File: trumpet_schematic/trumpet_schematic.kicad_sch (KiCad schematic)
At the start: 17 parts, among them J1 LCD, Q1 NPN, SW1 SW_Push, SW10 SW_Push, SW2 SW_Push, SW3 SW_Push, SW4 SW_Push, SW5 SW_Push, SW6 SW_Push, SW7 SW_Push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

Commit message: song array (swappable)
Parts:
- R2: value R -> 20Ω
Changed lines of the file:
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@@
 			)
 		)
-		(property "Value" "R"
+		(property "Value" "20Ω"
 			(at 77.47 99.06 90)
 			(effects

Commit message: lcd start
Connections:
- net VCC: no longer J1.VDD (Pin_2), R3.2, R4.1
- new net VCC 5V: J1.VDD (Pin_2), R3.2, R4.1
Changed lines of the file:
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@@
 		)
 	)
-	(label "VCC"
+	(label "VCC 5V"
 		(at 152.4 81.28 0)
 		(effects

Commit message: lcd progress
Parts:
- removed R3: 5kΩ, symbol Device:R
- added R5: R_Variable, symbol Device:R_Variable
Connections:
- net VCC 5V: now also R5.1
- net at J1.VO (Pin_3): now also R5.2
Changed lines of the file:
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@@
+	)
+	(symbol
+		(lib_id "Device:R_Variable")
+		(at 161.29 91.44 90)
+		(unit 1)
+		(exclude_from_sim no)
+		(in_bom yes)
+		(on_board yes)
+		(dnp no)
+		(fields_autoplaced yes)
+		(property "Reference" "R5"
+			(at 161.29 83.82 90)
+			(effects
+				(font
+					(size 1.27 1.27)
+				)
+			)
+		)
+		(property "Value" "R_Variable"
+			(at 161.29 86.36 90)
+			(effects
+				(font
+					(size 1.27 1.27)
+				)
+			)
+		)
+		(property "Footprint" ""
+			(at 161.29 93.218 90)
+			(effects
+				(font
+					(size 1.27 1.27)
+				)
+				(hide yes)
+			)
+		)
+		(property "Datasheet" "~"
+			(at 161.29 91.44 0)
+			(effects
+				(font
+					(size 1.27 1.27)
+				)
+				(hide yes)
+			)
+		)
+		(property "Description" "Variable resistor"
+			(at 161.29 91.44 0)
+			(effects
+				(font
+					(size 1.27 1.27)
+				)
+				(hide yes)
+			)
+		)
+		(pin "1"
+		)
+		(pin "2"
+		)
+		(instances
+			(project ""
+				(path "/72e6d7f3-c76a-4c03-a31b-775dd92d8425"
+					(reference "R5")
+					(unit 1)
+				)
+			)
+		)
 	)
 	(symbol
@@
 					(unit 1)
 				)
-			)
-		)
-	)
-	(symbol
-		(lib_id "Device:R")
-		(at 161.29 91.44 270)
-		(unit 1)
-		(exclude_from_sim no)
-		(in_bom yes)
-		(on_board yes)
-		(dnp no)
-		(fields_autoplaced yes)
-		(property "Reference" "R3"
-			(at 161.29 85.09 90)
-			(effects
-				(font
-					(size 1.27 1.27)
-				)
-			)
-		)
-		(property "Value" "5kΩ"
-			(at 161.29 87.63 90)
-			(effects
-				(font
-					(size 1.27 1.27)
-				)
-			)
-		)
-		(property "Footprint" ""
-			(at 161.29 89.662 90)
-			(effects
-				(font
-					(size 1.27 1.27)
-				)
-				(hide yes)
-			)
-		)
-		(property "Datasheet" "~"
-			(at 161.29 91.44 0)
-			(effects
-				(font
-					(size 1.27 1.27)
-				)
-				(hide yes)
-			)
-		)
-		(property "Description" "Resistor"
-			(at 161.29 91.44 0)
-			(effects
-				(font
-					(size 1.27 1.27)
-				)
-				(hide yes)
-			)
-		)
-		(pin "1"
-		)
-		(pin "2"
-		)
-		(instances
-			(project ""
-				(path "/72e6d7f3-c76a-4c03-a31b-775dd92d8425"
-					(reference "R3")
-					(unit 1)
-				)

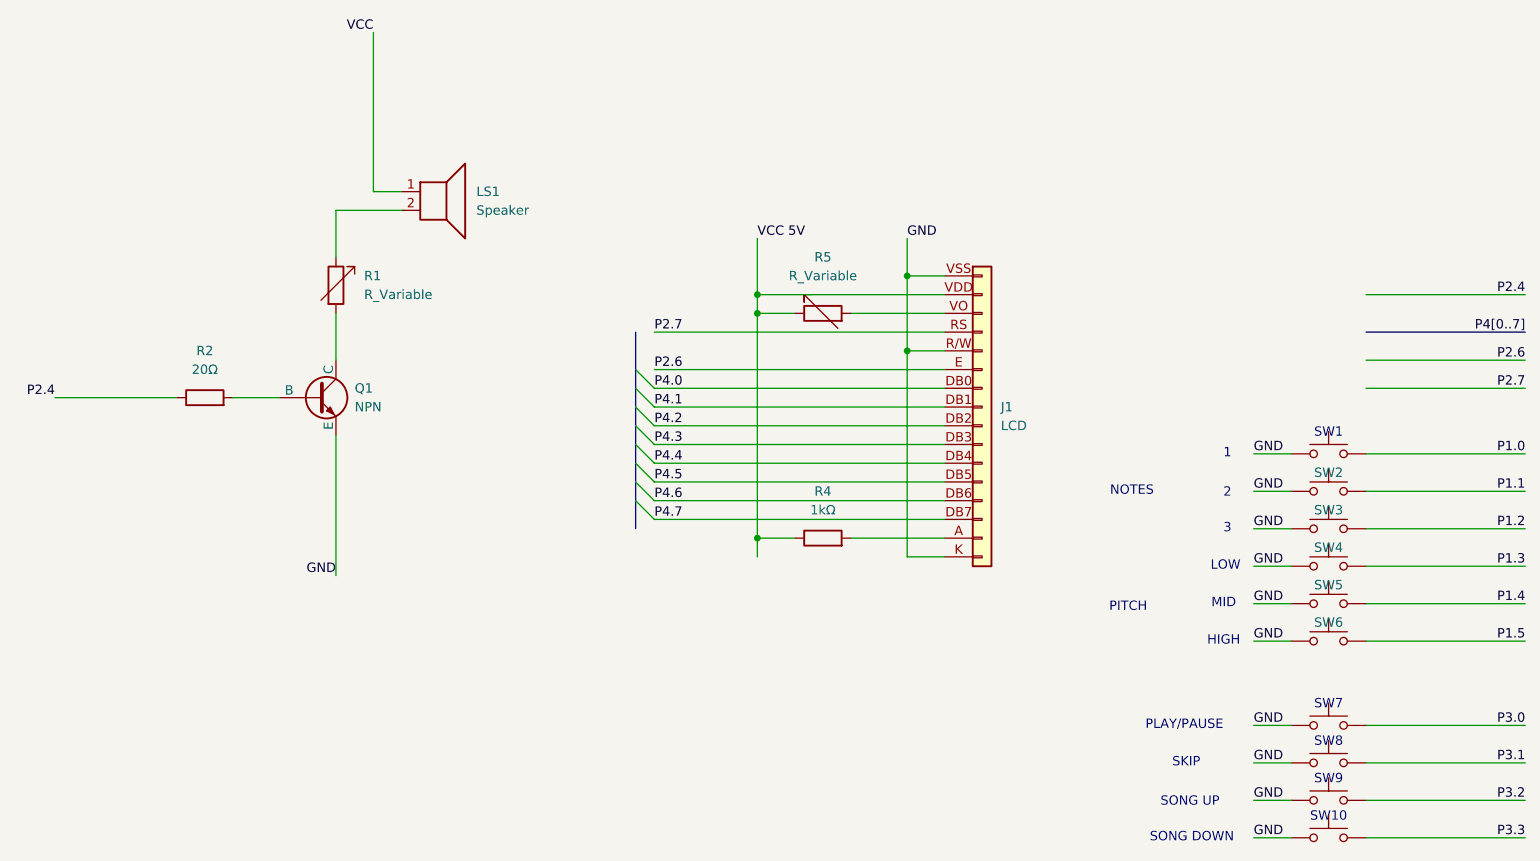
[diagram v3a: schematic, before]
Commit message: updated trumpet schematic and button assignments
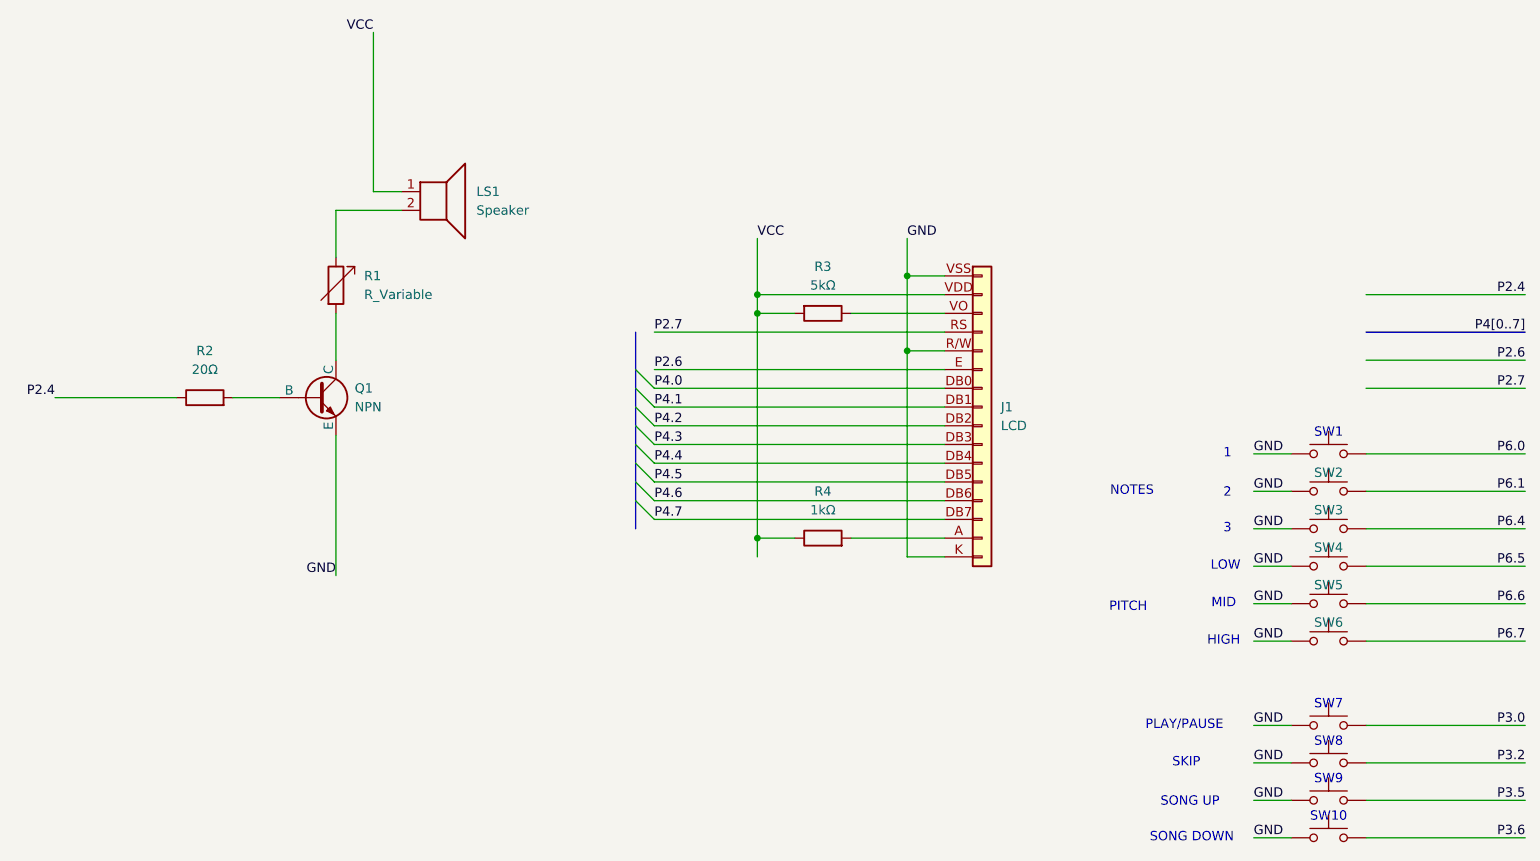
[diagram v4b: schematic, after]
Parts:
- removed R5: R_Variable, symbol Device:R_Variable
- added R3: 5kΩ, symbol Device:R
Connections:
- net P3.1 is gone; now on net P3.2: SW8.2
- net VCC 5V is gone; now on net VCC: J1.VDD (Pin_2), R4.1
- net P3.2: no longer SW9.2
- net VCC: now also R3.2
- net at J1.VO (Pin_3): now also R3.1
- net P1.0 renamed P6.0
- net P1.1 renamed P6.1
- net P1.2 renamed P6.4
- net P1.3 renamed P6.5
- net P1.4 renamed P6.6
- net P1.5 renamed P6.7
- net P3.3 renamed P3.6
- new net P3.5: SW9.2
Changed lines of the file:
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@@
 		)
 	)
-	(label "P3.1"
+	(label "P3.2"
 		(at 256.54 152.4 180)
 		(effects
@@
 		)
 	)
-	(label "P1.4"
+	(label "P6.6"
 		(at 256.54 130.81 180)
 		(effects
@@
 		)
 	)
-	(label "P1.3"
+	(label "P6.5"
 		(at 256.54 125.73 180)
 		(effects
@@
 		)
 	)
-	(label "P1.5"
+	(label "P6.7"
 		(at 256.54 135.89 180)
 		(effects
@@
 		)
 	)
-	(label "P1.1"
+	(label "P6.1"
 		(at 256.54 115.57 180)
 		(effects
@@
 		)
 	)
-	(label "P1.0"
+	(label "P6.0"
 		(at 256.54 110.49 180)
 		(effects
@@
 		)
 	)
-	(label "P1.2"
+	(label "P6.4"
 		(at 256.54 120.65 180)
 		(effects
@@
 		)
 	)
-	(label "P3.2"
+	(label "P3.5"
 		(at 256.54 157.48 180)
 		(effects
@@
 		)
 	)
-	(label "VCC 5V"
+	(label "VCC"
 		(at 152.4 81.28 0)
 		(effects
@@
 		)
 	)
-	(label "P3.3"
+	(label "P3.6"
 		(at 256.54 162.56 180)
 		(effects
@@
 	)
 	(symbol
-		(lib_id "Device:R_Variable")
-		(at 161.29 91.44 90)
-		(unit 1)
-		(exclude_from_sim no)
-		(in_bom yes)
-		(on_board yes)
-		(dnp no)
-		(fields_autoplaced yes)
-		(property "Reference" "R5"
-			(at 161.29 83.82 90)
-			(effects
-				(font
-					(size 1.27 1.27)
-				)
-			)
-		)
-		(property "Value" "R_Variable"
-			(at 161.29 86.36 90)
-			(effects
-				(font
-					(size 1.27 1.27)
-				)
-			)
-		)
-		(property "Footprint" ""
-			(at 161.29 93.218 90)
-			(effects
-				(font
-					(size 1.27 1.27)
-				)
-				(hide yes)
-			)
-		)
-		(property "Datasheet" "~"
-			(at 161.29 91.44 0)
-			(effects
-				(font
-					(size 1.27 1.27)
-				)
-				(hide yes)
-			)
-		)
-		(property "Description" "Variable resistor"
-			(at 161.29 91.44 0)
-			(effects
-				(font
-					(size 1.27 1.27)
-				)
-				(hide yes)
-			)
-		)
-		(pin "1"
-		)
-		(pin "2"
-		)
-		(instances
-			(project ""
-				(path "/72e6d7f3-c76a-4c03-a31b-775dd92d8425"
-					(reference "R5")
-					(unit 1)
-				)
-			)
-		)
-	)
-	(symbol
 		(lib_id "Switch:SW_Push")
 		(at 229.87 162.56 0)
@@
 					(unit 1)
 				)
+			)
+		)
+	)
+	(symbol
+		(lib_id "Device:R")
+		(at 161.29 91.44 270)
+		(unit 1)
+		(exclude_from_sim no)
+		(in_bom yes)
+		(on_board yes)
+		(dnp no)
+		(fields_autoplaced yes)
+		(property "Reference" "R3"
+			(at 161.29 85.09 90)
+			(effects
+				(font
+					(size 1.27 1.27)
+				)
+			)
+		)
+		(property "Value" "5kΩ"
+			(at 161.29 87.63 90)
+			(effects
+				(font
+					(size 1.27 1.27)
+				)
+			)
+		)
+		(property "Footprint" ""
+			(at 161.29 89.662 90)
+			(effects
+				(font
+					(size 1.27 1.27)
+				)
+				(hide yes)
+			)
+		)
+		(property "Datasheet" "~"
+			(at 161.29 91.44 0)
+			(effects
+				(font
+					(size 1.27 1.27)
+				)
+				(hide yes)
+			)
+		)
+		(property "Description" "Resistor"
+			(at 161.29 91.44 0)
+			(effects
+				(font
+					(size 1.27 1.27)
+				)
+				(hide yes)
+			)
+		)
+		(pin "1"
+		)
+		(pin "2"
+		)
+		(instances
+			(project ""
+				(path "/72e6d7f3-c76a-4c03-a31b-775dd92d8425"
+					(reference "R3")
+					(unit 1)
+				)
